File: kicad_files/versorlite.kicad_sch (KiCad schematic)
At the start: 0 parts

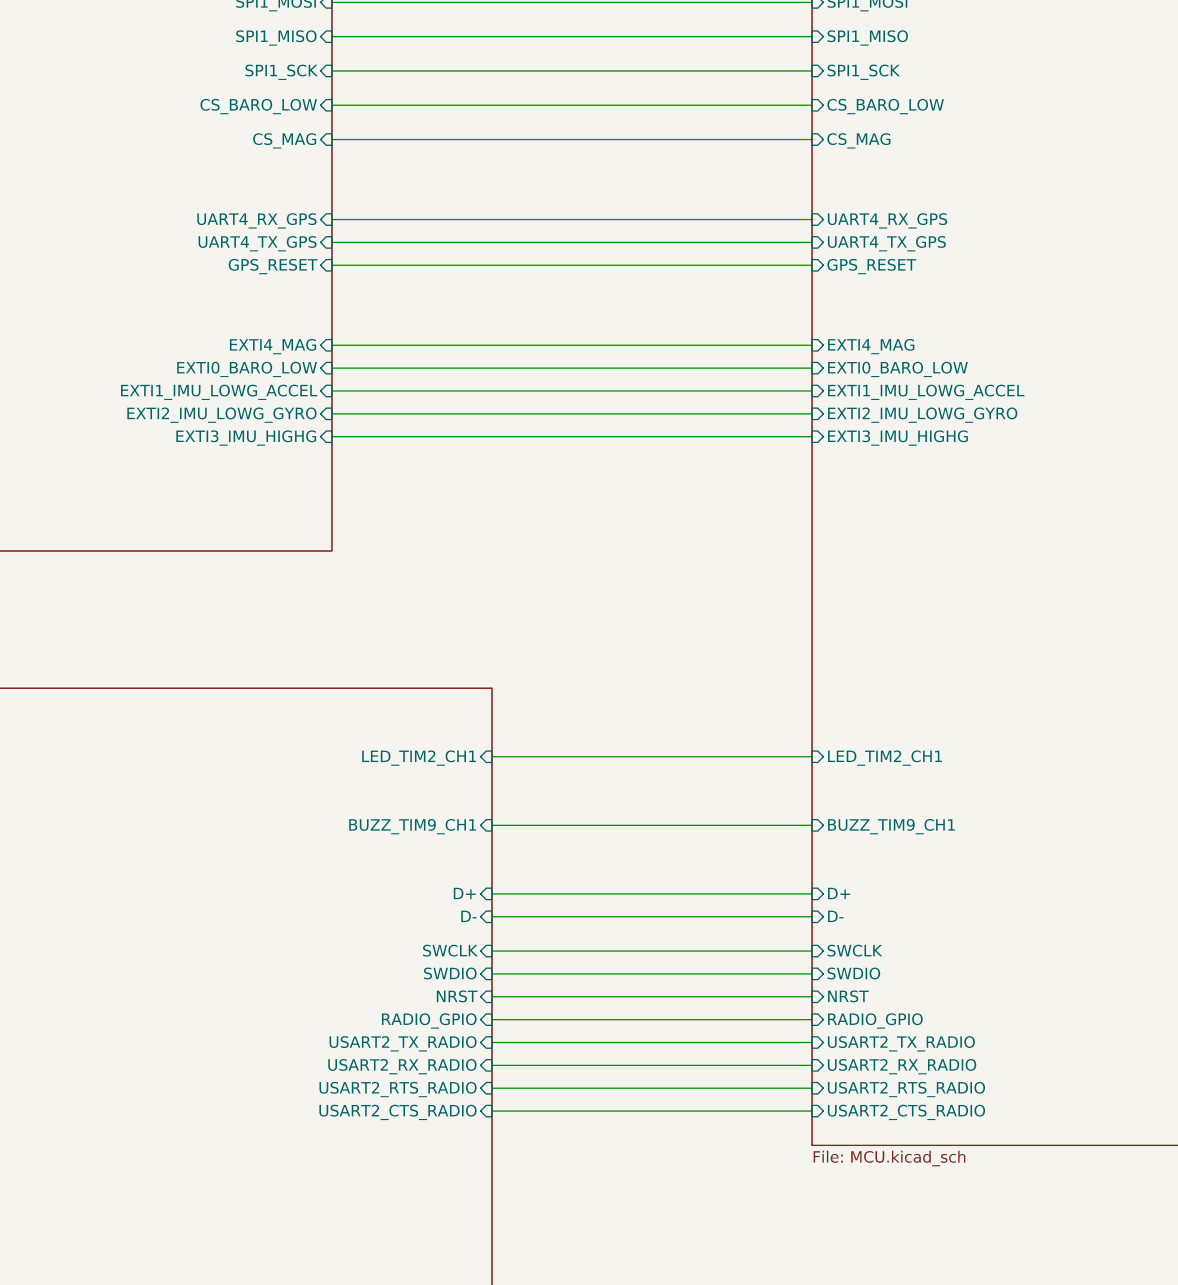
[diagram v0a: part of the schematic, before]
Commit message: switch uart, usart, spi lines, adc, pwm
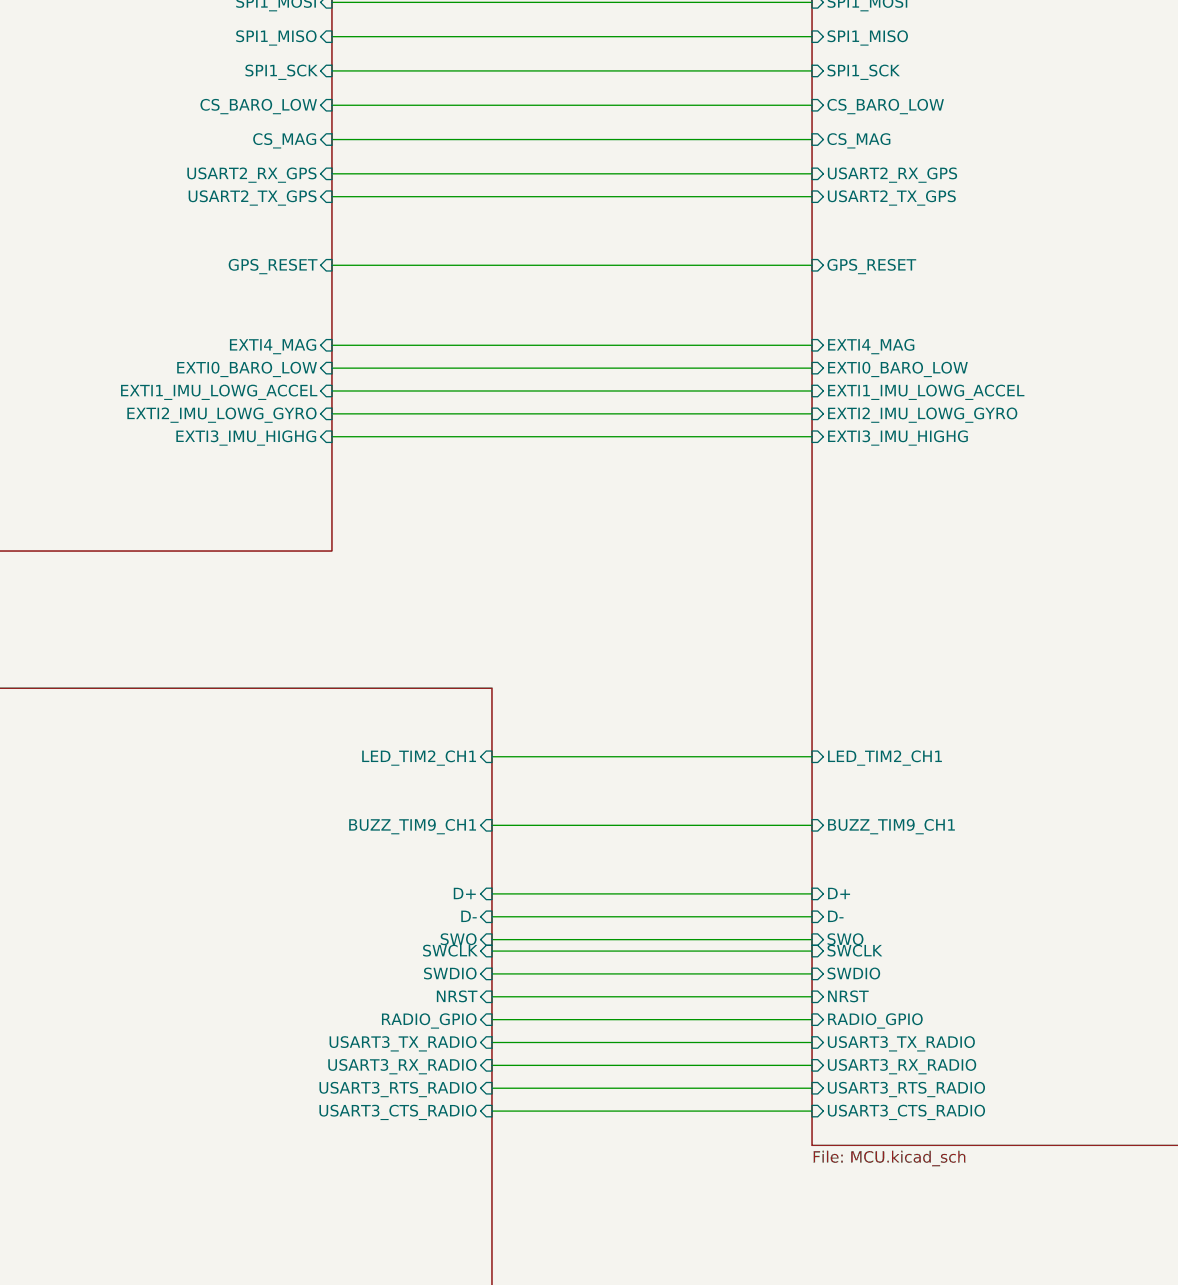
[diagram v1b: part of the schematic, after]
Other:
- sheet MCU ports: added SWO, USART2_RX_GPS, USART2_TX_GPS, USART3_CTS_RADIO, USART3_RTS_RADIO, USART3_RX_RADIO, USART3_TX_RADIO; removed UART4_RX_GPS, UART4_TX_GPS, USART2_CTS_RADIO, USART2_RTS_RADIO, USART2_RX_RADIO, USART2_TX_RADIO
- sheet Sensors ports: added USART2_RX_GPS, USART2_TX_GPS; removed UART4_RX_GPS, UART4_TX_GPS
- sheet Telemetry ports: added SWO, USART3_CTS_RADIO, USART3_RTS_RADIO, USART3_RX_RADIO, USART3_TX_RADIO; removed USART2_CTS_RADIO, USART2_RTS_RADIO, USART2_RX_RADIO, USART2_TX_RADIO
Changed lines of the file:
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@@
-	(wire
-		(pts
-			(xy 118.11 134.62) (xy 171.45 134.62)
-		)
-		(stroke
-			(width 0)
-			(type default)
-		)
-	)
 	(wire
 		(pts
@@
 	(wire
 		(pts
-			(xy 118.11 137.16) (xy 171.45 137.16)
+			(xy 118.11 129.54) (xy 171.45 129.54)
 		)
 		(stroke
@@
 	(wire
 		(pts
+			(xy 135.89 214.63) (xy 171.45 214.63)
+		)
+		(stroke
+			(width 0)
+			(type default)
+		)
+	)
+	(wire
+		(pts
 			(xy 118.11 156.21) (xy 171.45 156.21)
 		)
@@
 		(pts
 			(xy 306.07 88.9) (xy 306.07 93.98)
+		)
+		(stroke
+			(width 0)
+			(type default)
+		)
+	)
+	(wire
+		(pts
+			(xy 118.11 132.08) (xy 171.45 132.08)
 		)
 		(stroke
@@
 			)
 		)
-		(pin "UART4_RX_GPS" input
-			(at 118.11 134.62 0)
-			(effects
-				(font
-					(size 1.27 1.27)
-				)
-				(justify right)
-			)
-		)
-		(pin "UART4_TX_GPS" input
-			(at 118.11 137.16 0)
-			(effects
-				(font
-					(size 1.27 1.27)
-				)
-				(justify right)
-			)
-		)
 		(pin "GPS_RESET" input
 			(at 118.11 139.7 0)
+			(effects
+				(font
+					(size 1.27 1.27)
+				)
+				(justify right)
+			)
+		)
+		(pin "USART2_RX_GPS" input
+			(at 118.11 129.54 0)
+			(effects
+				(font
+					(size 1.27 1.27)
+				)
+				(justify right)
+			)
+		)
+		(pin "USART2_TX_GPS" input
+			(at 118.11 132.08 0)
 			(effects
 				(font
@@
 			)
 		)
-		(pin "USART2_CTS_RADIO" input
-			(at 135.89 233.68 0)
-			(effects
-				(font
-					(size 1.27 1.27)
-				)
-				(justify right)
-			)
-		)
-		(pin "USART2_RTS_RADIO" input
-			(at 135.89 231.14 0)
-			(effects
-				(font
-					(size 1.27 1.27)
-				)
-				(justify right)
-			)
-		)
-		(pin "USART2_RX_RADIO" input
-			(at 135.89 228.6 0)
-			(effects
-				(font
-					(size 1.27 1.27)
-				)
-				(justify right)
-			)
-		)
-		(pin "USART2_TX_RADIO" input
-			(at 135.89 226.06 0)
-			(effects
-				(font
-					(size 1.27 1.27)
-				)
-				(justify right)
-			)
-		)
 		(pin "NRST" input
 			(at 135.89 220.98 0)
@@
 		(pin "RADIO_GPIO" input
 			(at 135.89 223.52 0)
+			(effects
+				(font
+					(size 1.27 1.27)
+				)
+				(justify right)
+			)
+		)
+		(pin "SWO" input
+			(at 135.89 214.63 0)
+			(effects
+				(font
+					(size 1.27 1.27)
+				)
+				(justify right)
+			)
+		)
+		(pin "USART3_CTS_RADIO" input
+			(at 135.89 233.68 0)
+			(effects
+				(font
+					(size 1.27 1.27)
+				)
+				(justify right)
+			)
+		)
+		(pin "USART3_RTS_RADIO" input
+			(at 135.89 231.14 0)
+			(effects
+				(font
+					(size 1.27 1.27)
+				)
+				(justify right)
+			)
+		)
+		(pin "USART3_RX_RADIO" input
+			(at 135.89 228.6 0)
+			(effects
+				(font
+					(size 1.27 1.27)
+				)
+				(justify right)
+			)
+		)
+		(pin "USART3_TX_RADIO" input
+			(at 135.89 226.06 0)
 			(effects
 				(font
@@
 			)
 		)
-		(pin "UART4_RX_GPS" input
-			(at 171.45 134.62 180)
-			(effects
-				(font
-					(size 1.27 1.27)
-				)
-				(justify left)
-			)
-		)
-		(pin "UART4_TX_GPS" input
-			(at 171.45 137.16 180)
-			(effects
-				(font
-					(size 1.27 1.27)
-				)
-				(justify left)
-			)
-		)
-		(pin "USART2_CTS_RADIO" input
-			(at 171.45 233.68 180)
-			(effects
-				(font
-					(size 1.27 1.27)
-				)
-				(justify left)
-			)
-		)
-		(pin "USART2_RTS_RADIO" input
-			(at 171.45 231.14 180)
-			(effects
-				(font
-					(size 1.27 1.27)
-				)
-				(justify left)
-			)
-		)
-		(pin "USART2_RX_RADIO" input
-			(at 171.45 228.6 180)
-			(effects
-				(font
-					(size 1.27 1.27)
-				)
-				(justify left)
-			)
-		)
-		(pin "USART2_TX_RADIO" input
-			(at 171.45 226.06 180)
-			(effects
-				(font
-					(size 1.27 1.27)
-				)
-				(justify left)
-			)
-		)
 		(pin "IGN_ADC" input
 			(at 274.32 97.79 0)
@@
 			)
 		)
+		(pin "SWO" input
+			(at 171.45 214.63 180)
+			(effects
+				(font
+					(size 1.27 1.27)
+				)
+				(justify left)
+			)
+		)
+		(pin "USART3_CTS_RADIO" input
+			(at 171.45 233.68 180)
+			(effects
+				(font
+					(size 1.27 1.27)
+				)
+				(justify left)
+			)
+		)
+		(pin "USART3_RTS_RADIO" input
+			(at 171.45 231.14 180)
+			(effects
+				(font
+					(size 1.27 1.27)
+				)
+				(justify left)
+			)
+		)
+		(pin "USART3_RX_RADIO" input
+			(at 171.45 228.6 180)
+			(effects
+				(font
+					(size 1.27 1.27)
+				)
+				(justify left)
+			)
+		)
+		(pin "USART3_TX_RADIO" input
+			(at 171.45 226.06 180)
+			(effects
+				(font
+					(size 1.27 1.27)
+				)
+				(justify left)
+			)
+		)
+		(pin "USART2_RX_GPS" input
+			(at 171.45 129.54 180)
+			(effects
+				(font
+					(size 1.27 1.27)
+				)
+				(justify left)
+			)
+		)
+		(pin "USART2_TX_GPS" input
+			(at 171.45 132.08 180)
+			(effects
+				(font
+					(size 1.27 1.27)
+				)
+				(justify left)
+			)
+		)

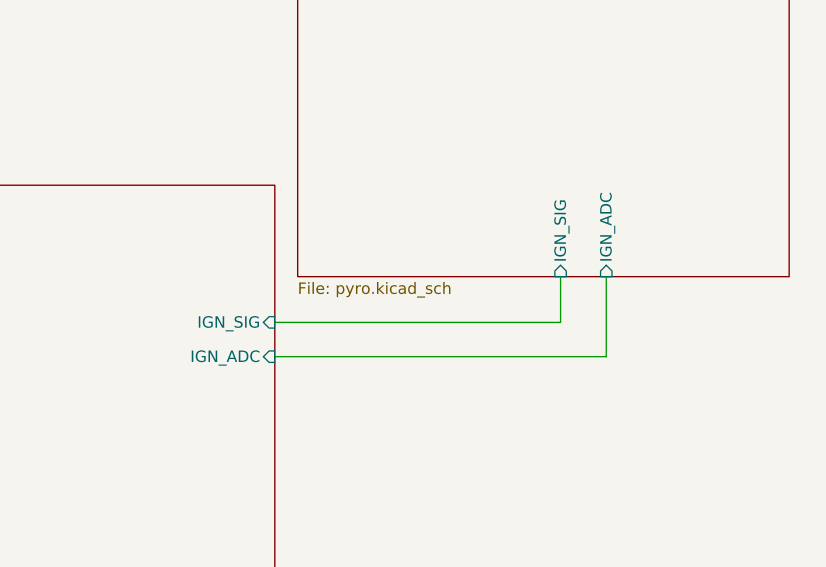
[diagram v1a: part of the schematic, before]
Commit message: Connect IGN2 signal, rearrange
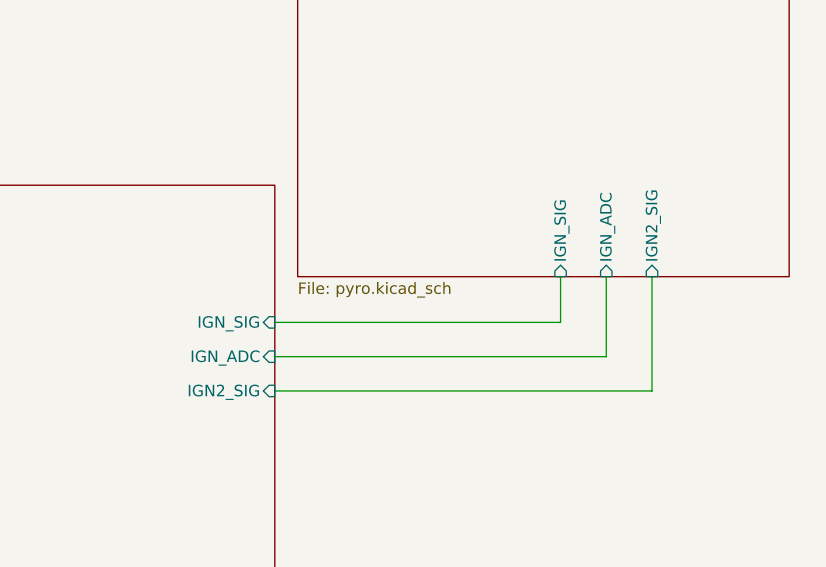
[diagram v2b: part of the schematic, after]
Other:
- sheet MCU ports: added IGN2_SIG; removed none
- sheet Pyro ports: added IGN2_SIG; removed none
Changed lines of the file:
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@@
+	(wire
+		(pts
+			(xy 316.23 88.9) (xy 316.23 101.6)
+		)
+		(stroke
+			(width 0)
+			(type default)
+		)
+	)
 	(wire
 		(pts
@@
 		(pts
 			(xy 306.07 88.9) (xy 306.07 93.98)
+		)
+		(stroke
+			(width 0)
+			(type default)
+		)
+	)
+	(wire
+		(pts
+			(xy 274.32 101.6) (xy 316.23 101.6)
 		)
 		(stroke
@@
 			)
 		)
+		(pin "IGN2_SIG" input
+			(at 274.32 101.6 0)
+			(effects
+				(font
+					(size 1.27 1.27)
+				)
+				(justify right)
+			)
+		)
 		(instances
 			(project "versorlite"
@@
 			(effects
 				(font
+					(size 1.27 1.27)
+				)
+				(justify left)
+			)
+		)
+		(pin "IGN2_SIG" input
+			(at 316.23 88.9 270)
+			(effects
+				(font

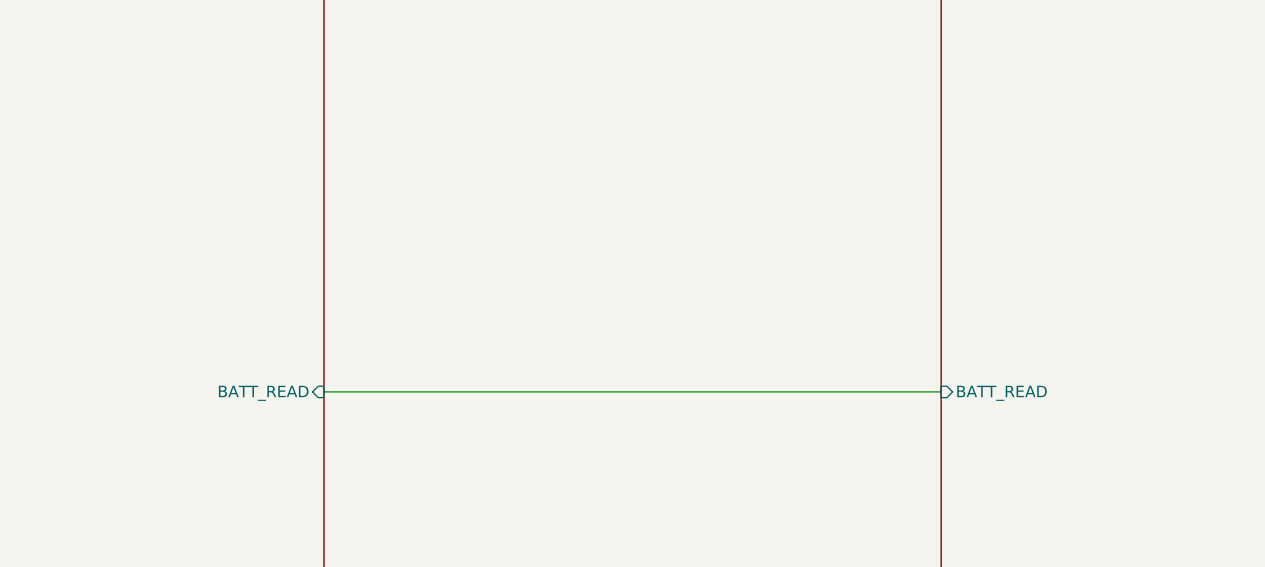
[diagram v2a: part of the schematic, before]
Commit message: add dedicated power switching
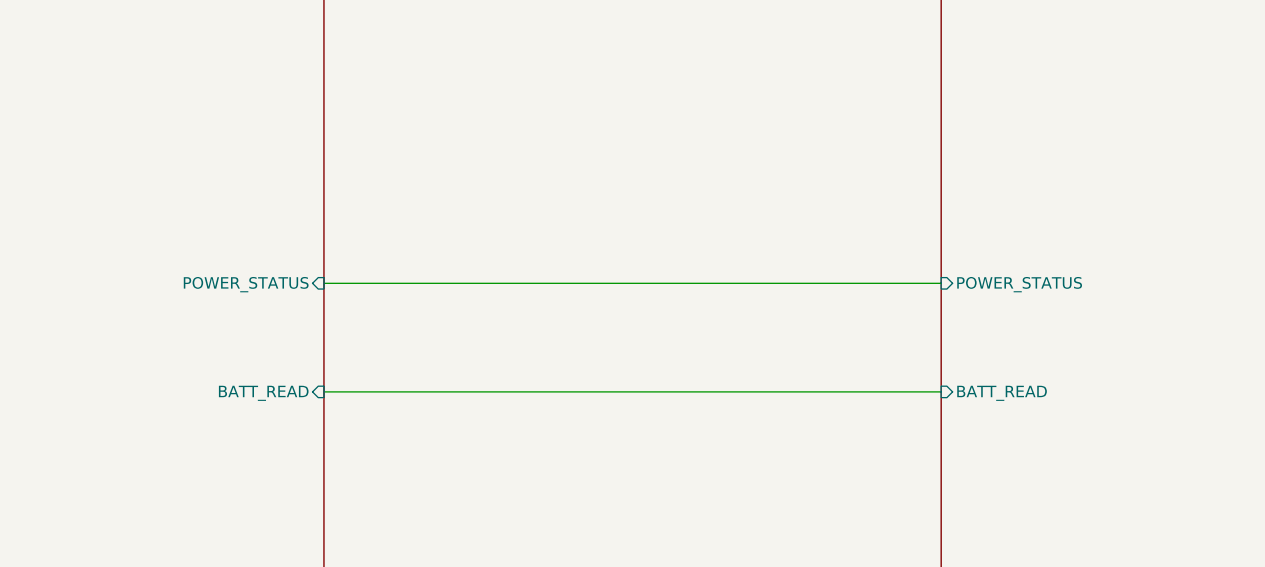
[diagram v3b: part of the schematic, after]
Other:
- sheet MCU ports: added POWER_STATUS; removed none
- sheet Power ports: added POWER_STATUS; removed none
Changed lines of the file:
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@@
+	(wire
+		(pts
+			(xy 274.32 191.135) (xy 342.9 191.135)
+		)
+		(stroke
+			(width 0)
+			(type default)
+		)
+	)
 	(wire
 		(pts
@@
 			)
 		)
+		(pin "POWER_STATUS" input
+			(at 342.9 191.135 180)
+			(effects
+				(font
+					(size 1.27 1.27)
+				)
+				(justify left)
+			)
+		)
 		(instances
 			(project "versorlite"
@@
 			(effects
 				(font
+					(size 1.27 1.27)
+				)
+				(justify right)
+			)
+		)
+		(pin "POWER_STATUS" input
+			(at 274.32 191.135 0)
+			(effects
+				(font

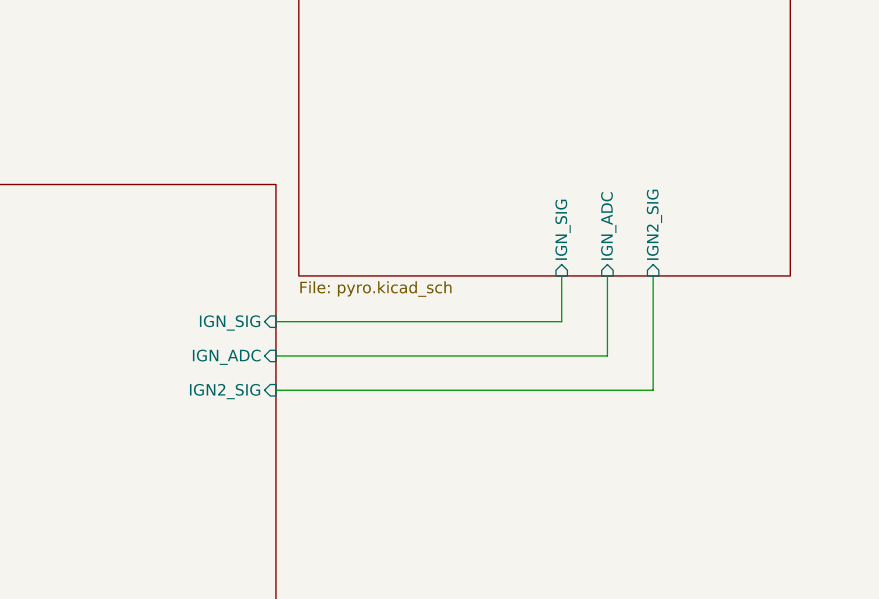
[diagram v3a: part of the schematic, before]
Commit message: add ign_adc2
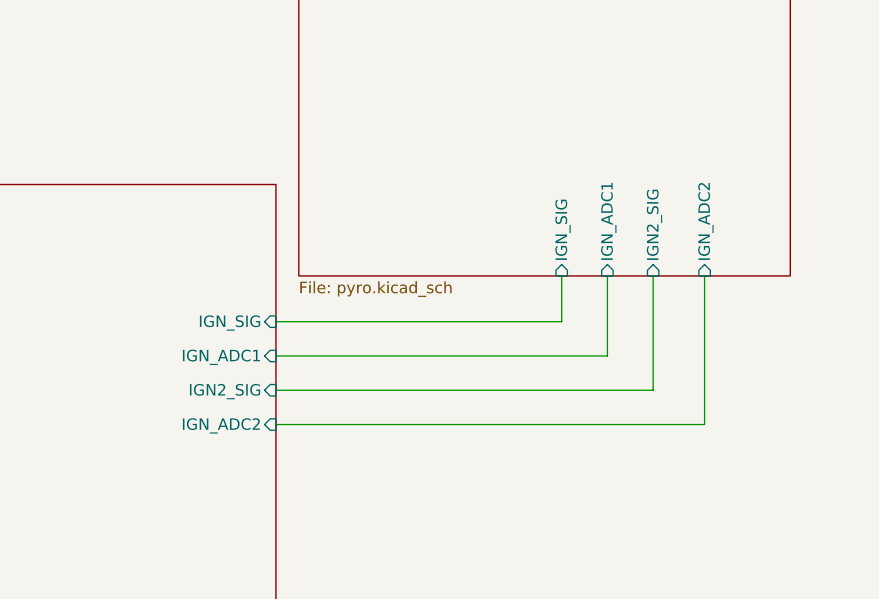
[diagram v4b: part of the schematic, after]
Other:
- sheet MCU ports: added IGN_ADC1, IGN_ADC2; removed IGN_ADC
- sheet Pyro ports: added IGN_ADC1, IGN_ADC2; removed IGN_ADC
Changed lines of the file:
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@@
+	(wire
+		(pts
+			(xy 321.945 105.41) (xy 274.32 105.41)
+		)
+		(stroke
+			(width 0)
+			(type default)
+		)
+	)
 	(wire
 		(pts
@@
 		(pts
 			(xy 118.11 132.08) (xy 171.45 132.08)
+		)
+		(stroke
+			(width 0)
+			(type default)
+		)
+	)
+	(wire
+		(pts
+			(xy 321.945 88.9) (xy 321.945 105.41)
 		)
 		(stroke
@@
 			)
 		)
-		(pin "IGN_ADC" input
-			(at 274.32 97.79 0)
-			(effects
-				(font
-					(size 1.27 1.27)
-				)
-				(justify right)
-			)
-		)
 		(pin "GPS_RESET" input
 			(at 171.45 139.7 180)
@@
 		(pin "POWER_STATUS" input
 			(at 274.32 191.135 0)
+			(effects
+				(font
+					(size 1.27 1.27)
+				)
+				(justify right)
+			)
+		)
+		(pin "IGN_ADC1" input
+			(at 274.32 97.79 0)
+			(effects
+				(font
+					(size 1.27 1.27)
+				)
+				(justify right)
+			)
+		)
+		(pin "IGN_ADC2" input
+			(at 274.32 105.41 0)
 			(effects
 				(font
@@
 			)
 		)
-		(pin "IGN_ADC" input
-			(at 311.15 88.9 270)
-			(effects
-				(font
-					(size 1.27 1.27)
-				)
-				(justify left)
-			)
-		)
 		(pin "IGN2_SIG" input
 			(at 316.23 88.9 270)
 			(effects
 				(font
+					(size 1.27 1.27)
+				)
+				(justify left)
+			)
+		)
+		(pin "IGN_ADC1" input
+			(at 311.15 88.9 270)
+			(effects
+				(font
+					(size 1.27 1.27)
+				)
+				(justify left)
+			)
+		)
+		(pin "IGN_ADC2" input
+			(at 321.945 88.9 270)
+			(effects
+				(font
